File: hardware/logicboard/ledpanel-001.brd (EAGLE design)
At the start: 16 x 27 mm, 7 parts

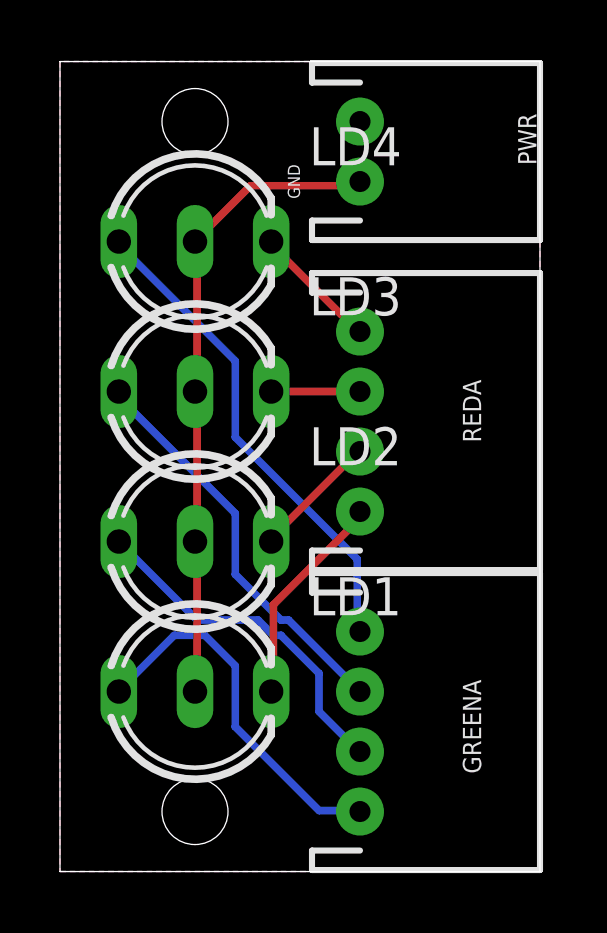
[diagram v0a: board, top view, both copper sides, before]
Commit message: Changed dimension.
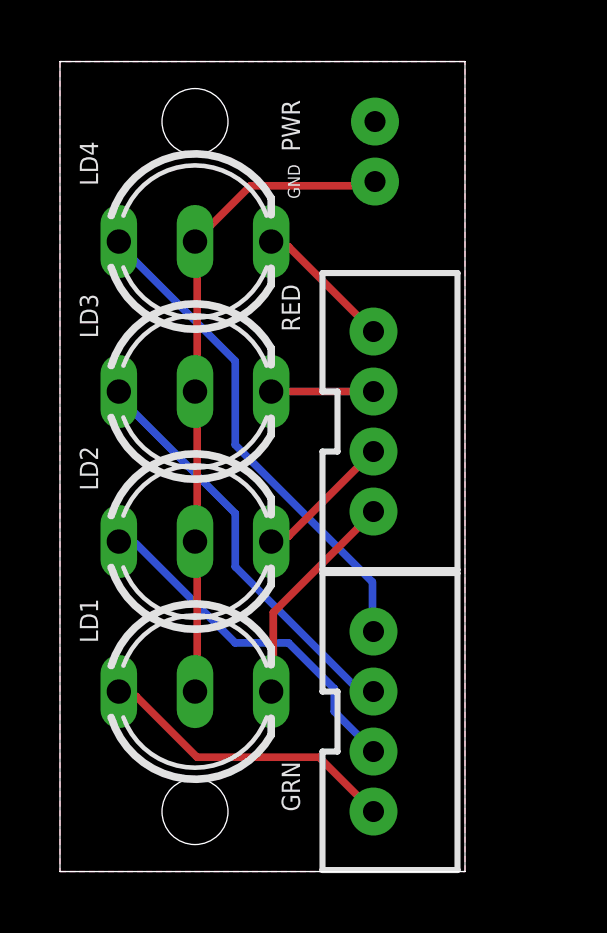
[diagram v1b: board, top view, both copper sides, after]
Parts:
- removed GREENA, REDA: (no value), SparkFun-Connectors:JST-4-PTH
- added GRN, RED: (no value), SparkFun-Connectors:JST-4-PTH-VERT
- PWR: device SparkFun-Connectors:JST-2-PTH -> SparkFun-Connectors:JST-2-PTH-NS
- moved PWR 0.50 mm to (10.5, 24.0)
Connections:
- net GREEN1: now also GRN.1; no longer GREENA.1
- net GREEN2: now also GRN.2; no longer GREENA.2
- net GREEN3: now also GRN.3; no longer GREENA.3
- net GREEN4: now also GRN.4; no longer GREENA.4
- net RED1: now also RED.1; no longer REDA.1
- net RED2: now also RED.2; no longer REDA.2
- net RED3: now also RED.3; no longer REDA.3
- net RED4: now also RED.4; no longer REDA.4
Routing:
- net GREEN4: track 12.4 -> 10.2 mm
- net GND: track 21.5 -> 22.0 mm
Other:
- board size 16 x 27 mm -> 13.5 x 27 mm
